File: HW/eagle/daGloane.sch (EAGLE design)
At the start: 110 parts, among them IC1 MCP1252-33X50, U1 STM32F10XTXU6, X2 SPARKFUN-CONNECTORS_USB-MICROB

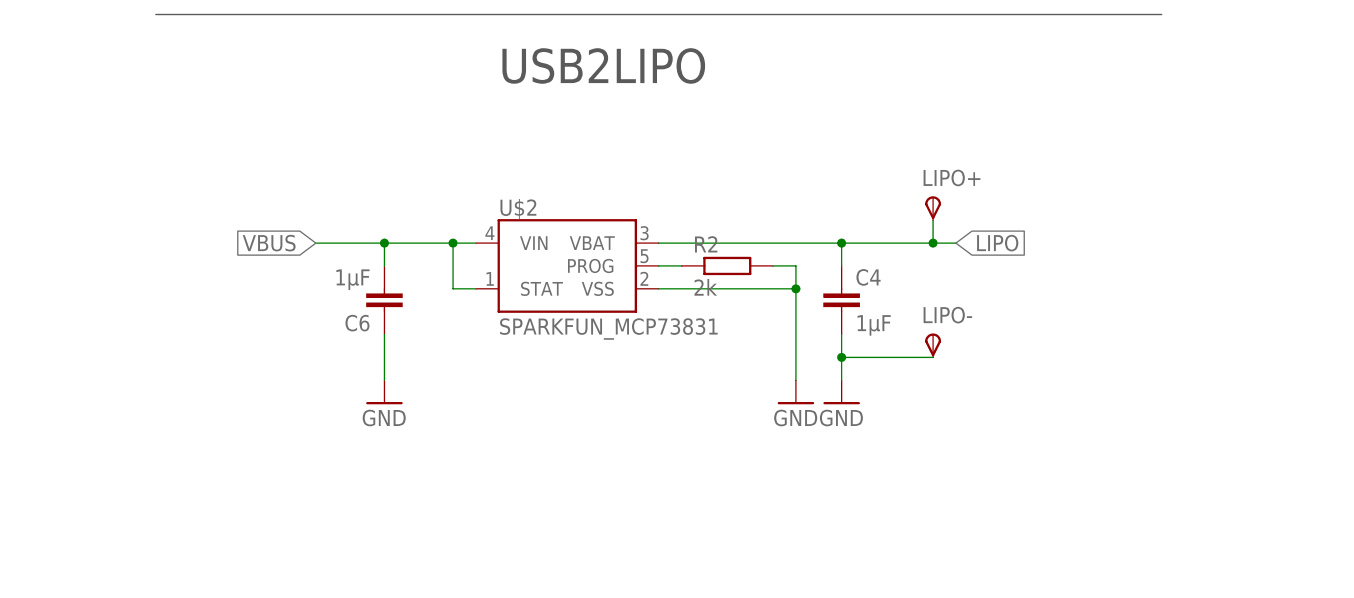
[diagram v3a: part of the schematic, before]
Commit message: led added to LiPo charge IC
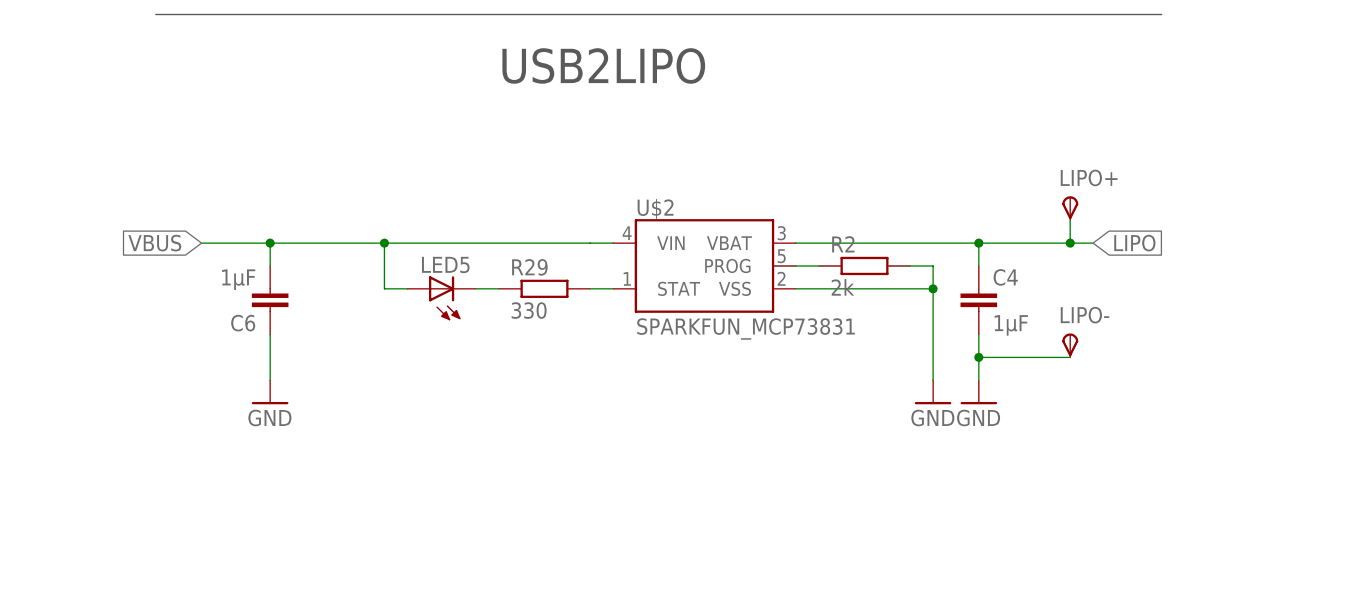
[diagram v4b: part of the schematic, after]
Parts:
- added LED5: (no value), led:LEDCHIPLED_0805
- added R29: 330, rcl:R-EU_R0603
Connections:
- new net N$43: R29.2, U$2.STAT
- new net N$44: LED5.C, R29.1
- net VBUS: now also LED5.A; no longer U$2.STAT
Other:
- moved on the sheet: C4, C6, LIPO+, LIPO-, R2, U$2
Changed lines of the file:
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@@
 <part name="R28" library="rcl" deviceset="R-EU_" device="R0603" value="10k"/>
 <part name="D5" library="diode" deviceset="MBR0520LT" device=""/>
+<part name="LED5" library="led" deviceset="LED" device="CHIPLED_0805"/>
+<part name="R29" library="rcl" deviceset="R-EU_" device="R0603" value="330"/>
 </parts>
 <sheets>
@@
 <instance part="LED1" gate="G$1" x="149.86" y="-355.6" rot="R270"/>
 <instance part="LED2" gate="G$1" x="149.86" y="-365.76" rot="R270"/>
-<instance part="U$2" gate="G$1" x="68.58" y="-167.64"/>
-<instance part="C6" gate="G$1" x="48.26" y="-172.72" rot="R180"/>
-<instance part="GND28" gate="1" x="48.26" y="-182.88"/>
-<instance part="GND29" gate="1" x="93.98" y="-182.88"/>
-<instance part="C4" gate="G$1" x="99.06" y="-170.18"/>
-<instance part="GND30" gate="1" x="99.06" y="-182.88"/>
-<instance part="LIPO+" gate="G$1" x="109.22" y="-160.02"/>
-<instance part="LIPO-" gate="G$1" x="109.22" y="-175.26"/>
-<instance part="R2" gate="G$1" x="86.36" y="-167.64"/>
+<instance part="U$2" gate="G$1" x="83.82" y="-167.64"/>
+<instance part="C6" gate="G$1" x="35.56" y="-172.72" rot="R180"/>
+<instance part="GND28" gate="1" x="35.56" y="-182.88"/>
+<instance part="GND29" gate="1" x="109.22" y="-182.88"/>
+<instance part="C4" gate="G$1" x="114.3" y="-170.18"/>
+<instance part="GND30" gate="1" x="114.3" y="-182.88"/>
+<instance part="LIPO+" gate="G$1" x="124.46" y="-160.02"/>
+<instance part="LIPO-" gate="G$1" x="124.46" y="-175.26"/>
+<instance part="R2" gate="G$1" x="101.6" y="-167.64"/>
 <instance part="IC1" gate="G$1" x="218.44" y="-78.74"/>
 <instance part="C13" gate="G$1" x="243.84" y="-81.28"/>
@@
 <instance part="R28" gate="G$1" x="462.28" y="-340.36"/>
 <instance part="D5" gate="G$1" x="472.44" y="-317.5" rot="R90"/>
+<instance part="LED5" gate="G$1" x="53.34" y="-170.18" rot="R90"/>
+<instance part="R29" gate="G$1" x="66.04" y="-170.18"/>
 </instances>
 <busses>
@@
 <pinref part="C6" gate="G$1" pin="1"/>
 <pinref part="GND28" gate="1" pin="GND"/>
-<wire x1="48.26" y1="-180.34" x2="48.26" y2="-175.26" width="0.1524" layer="91"/>
+<wire x1="35.56" y1="-180.34" x2="35.56" y2="-175.26" width="0.1524" layer="91"/>
 </segment>
 <segment>
-<wire x1="93.98" y1="-167.64" x2="93.98" y2="-170.18" width="0.1524" layer="91"/>
+<wire x1="109.22" y1="-167.64" x2="109.22" y2="-170.18" width="0.1524" layer="91"/>
 <pinref part="U$2" gate="G$1" pin="VSS"/>
-<wire x1="78.74" y1="-170.18" x2="93.98" y2="-170.18" width="0.1524" layer="91"/>
-<wire x1="93.98" y1="-170.18" x2="93.98" y2="-180.34" width="0.1524" layer="91"/>
-<junction x="93.98" y="-170.18"/>
+<wire x1="93.98" y1="-170.18" x2="109.22" y2="-170.18" width="0.1524" layer="91"/>
+<wire x1="109.22" y1="-170.18" x2="109.22" y2="-180.34" width="0.1524" layer="91"/>
+<junction x="109.22" y="-170.18"/>
 <pinref part="GND29" gate="1" pin="GND"/>
 <pinref part="R2" gate="G$1" pin="2"/>
-<wire x1="91.44" y1="-167.64" x2="93.98" y2="-167.64" width="0.1524" layer="91"/>
+<wire x1="106.68" y1="-167.64" x2="109.22" y2="-167.64" width="0.1524" layer="91"/>
 </segment>
 <segment>
 <pinref part="GND30" gate="1" pin="GND"/>
 <pinref part="C4" gate="G$1" pin="2"/>
-<wire x1="99.06" y1="-180.34" x2="99.06" y2="-177.8" width="0.1524" layer="91"/>
+<wire x1="114.3" y1="-180.34" x2="114.3" y2="-177.8" width="0.1524" layer="91"/>
 <pinref part="LIPO-" gate="G$1" pin="PP"/>
-<wire x1="99.06" y1="-177.8" x2="99.06" y2="-175.26" width="0.1524" layer="91"/>
-<wire x1="109.22" y1="-177.8" x2="99.06" y2="-177.8" width="0.1524" layer="91"/>
-<junction x="99.06" y="-177.8"/>
+<wire x1="114.3" y1="-177.8" x2="114.3" y2="-175.26" width="0.1524" layer="91"/>
+<wire x1="124.46" y1="-177.8" x2="114.3" y2="-177.8" width="0.1524" layer="91"/>
+<junction x="114.3" y="-177.8"/>
 </segment>
 <segment>
@@
 <segment>
 <pinref part="C4" gate="G$1" pin="1"/>
-<wire x1="99.06" y1="-167.64" x2="99.06" y2="-165.1" width="0.1524" layer="91"/>
+<wire x1="114.3" y1="-167.64" x2="114.3" y2="-165.1" width="0.1524" layer="91"/>
 <pinref part="U$2" gate="G$1" pin="VBAT"/>
-<wire x1="99.06" y1="-165.1" x2="78.74" y2="-165.1" width="0.1524" layer="91"/>
-<wire x1="99.06" y1="-165.1" x2="109.22" y2="-165.1" width="0.1524" layer="91"/>
-<junction x="99.06" y="-165.1"/>
-<label x="111.76" y="-165.1" size="1.778" layer="95" xref="yes"/>
+<wire x1="114.3" y1="-165.1" x2="93.98" y2="-165.1" width="0.1524" layer="91"/>
+<wire x1="114.3" y1="-165.1" x2="124.46" y2="-165.1" width="0.1524" layer="91"/>
+<junction x="114.3" y="-165.1"/>
+<label x="127" y="-165.1" size="1.778" layer="95" xref="yes"/>
 <pinref part="LIPO+" gate="G$1" pin="PP"/>
-<wire x1="109.22" y1="-165.1" x2="111.76" y2="-165.1" width="0.1524" layer="91"/>
-<wire x1="109.22" y1="-162.56" x2="109.22" y2="-165.1" width="0.1524" layer="91"/>
-<junction x="109.22" y="-165.1"/>
+<wire x1="124.46" y1="-165.1" x2="127" y2="-165.1" width="0.1524" layer="91"/>
+<wire x1="124.46" y1="-162.56" x2="124.46" y2="-165.1" width="0.1524" layer="91"/>
+<junction x="124.46" y="-165.1"/>
 </segment>
 <segment>
@@
 </segment>
 <segment>
-<pinref part="U$2" gate="G$1" pin="STAT"/>
-<wire x1="58.42" y1="-170.18" x2="55.88" y2="-170.18" width="0.1524" layer="91"/>
-<wire x1="55.88" y1="-170.18" x2="55.88" y2="-165.1" width="0.1524" layer="91"/>
 <pinref part="U$2" gate="G$1" pin="VIN"/>
-<wire x1="55.88" y1="-165.1" x2="58.42" y2="-165.1" width="0.1524" layer="91"/>
-<wire x1="55.88" y1="-165.1" x2="48.26" y2="-165.1" width="0.1524" layer="91"/>
-<junction x="55.88" y="-165.1"/>
+<wire x1="71.12" y1="-165.1" x2="73.66" y2="-165.1" width="0.1524" layer="91"/>
+<wire x1="71.12" y1="-165.1" x2="48.26" y2="-165.1" width="0.1524" layer="91"/>
 <pinref part="C6" gate="G$1" pin="2"/>
-<wire x1="48.26" y1="-165.1" x2="48.26" y2="-167.64" width="0.1524" layer="91"/>
-<wire x1="48.26" y1="-165.1" x2="40.64" y2="-165.1" width="0.1524" layer="91"/>
+<wire x1="48.26" y1="-165.1" x2="35.56" y2="-165.1" width="0.1524" layer="91"/>
+<wire x1="35.56" y1="-165.1" x2="35.56" y2="-167.64" width="0.1524" layer="91"/>
+<wire x1="35.56" y1="-165.1" x2="27.94" y2="-165.1" width="0.1524" layer="91"/>
+<junction x="35.56" y="-165.1"/>
+<label x="27.94" y="-165.1" size="1.778" layer="95" rot="R180" xref="yes"/>
+<pinref part="LED5" gate="G$1" pin="A"/>
+<wire x1="50.8" y1="-170.18" x2="48.26" y2="-170.18" width="0.1524" layer="91"/>
+<wire x1="48.26" y1="-170.18" x2="48.26" y2="-165.1" width="0.1524" layer="91"/>
 <junction x="48.26" y="-165.1"/>
-<label x="40.64" y="-165.1" size="1.778" layer="95" rot="R180" xref="yes"/>
 </segment>
 </net>
@@
 <pinref part="U$2" gate="G$1" pin="PROG"/>
 <pinref part="R2" gate="G$1" pin="1"/>
-<wire x1="81.28" y1="-167.64" x2="78.74" y2="-167.64" width="0.1524" layer="91"/>
+<wire x1="96.52" y1="-167.64" x2="93.98" y2="-167.64" width="0.1524" layer="91"/>
 </segment>
 </net>
@@
 </segment>
 </net>
+<net name="N$43" class="0">
+<segment>
+<pinref part="U$2" gate="G$1" pin="STAT"/>
+<pinref part="R29" gate="G$1" pin="2"/>
+<wire x1="71.12" y1="-170.18" x2="73.66" y2="-170.18" width="0.1524" layer="91"/>
+</segment>
+</net>
+<net name="N$44" class="0">
+<segment>
+<pinref part="R29" gate="G$1" pin="1"/>
+<pinref part="LED5" gate="G$1" pin="C"/>
+<wire x1="58.42" y1="-170.18" x2="60.96" y2="-170.18" width="0.1524" layer="91"/>
+</segment>
+</net>

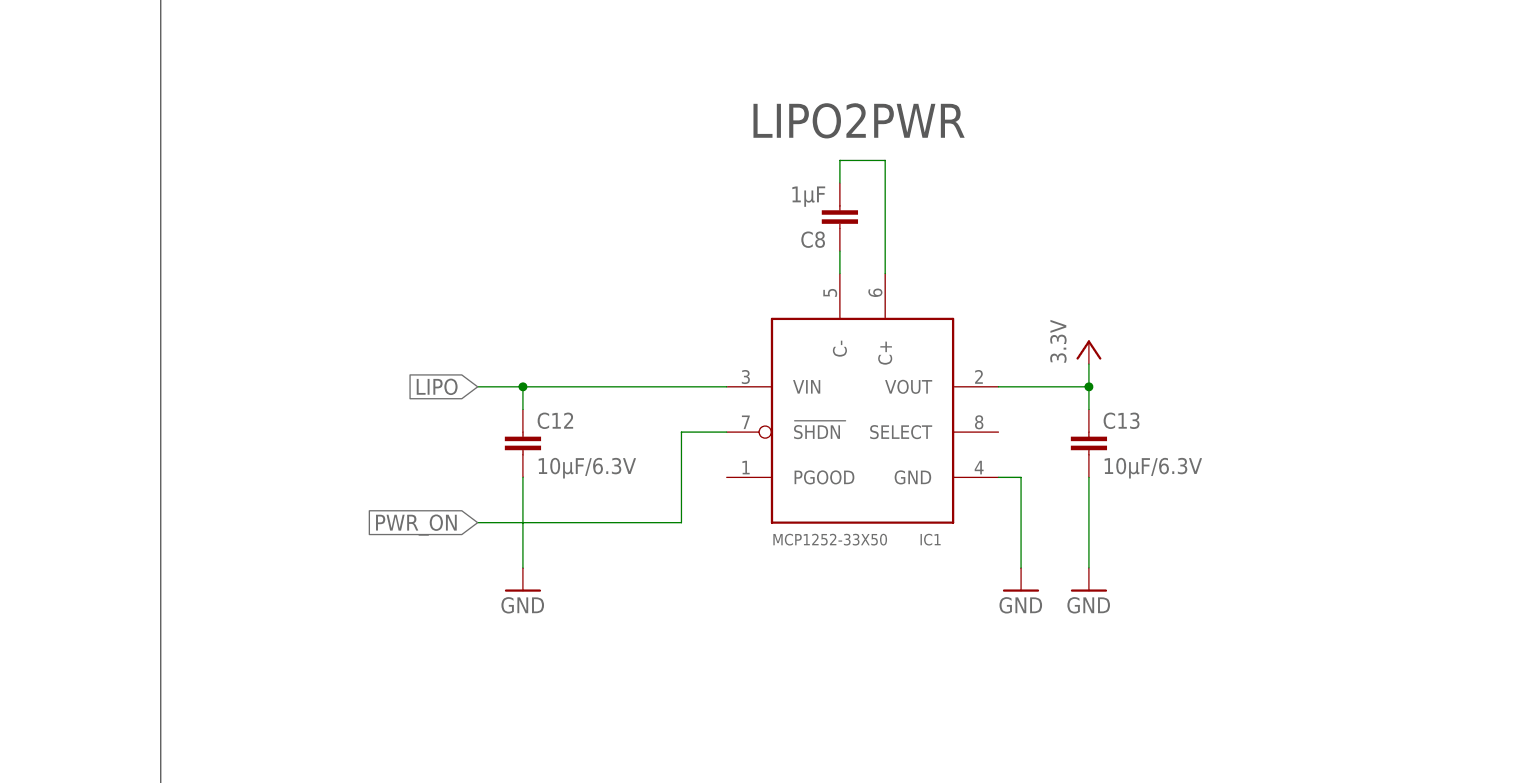
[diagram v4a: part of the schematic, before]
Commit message: - PI filter added to charge pump DC/DC - trough hole pads for BLDC motors replaced with SMT type pads
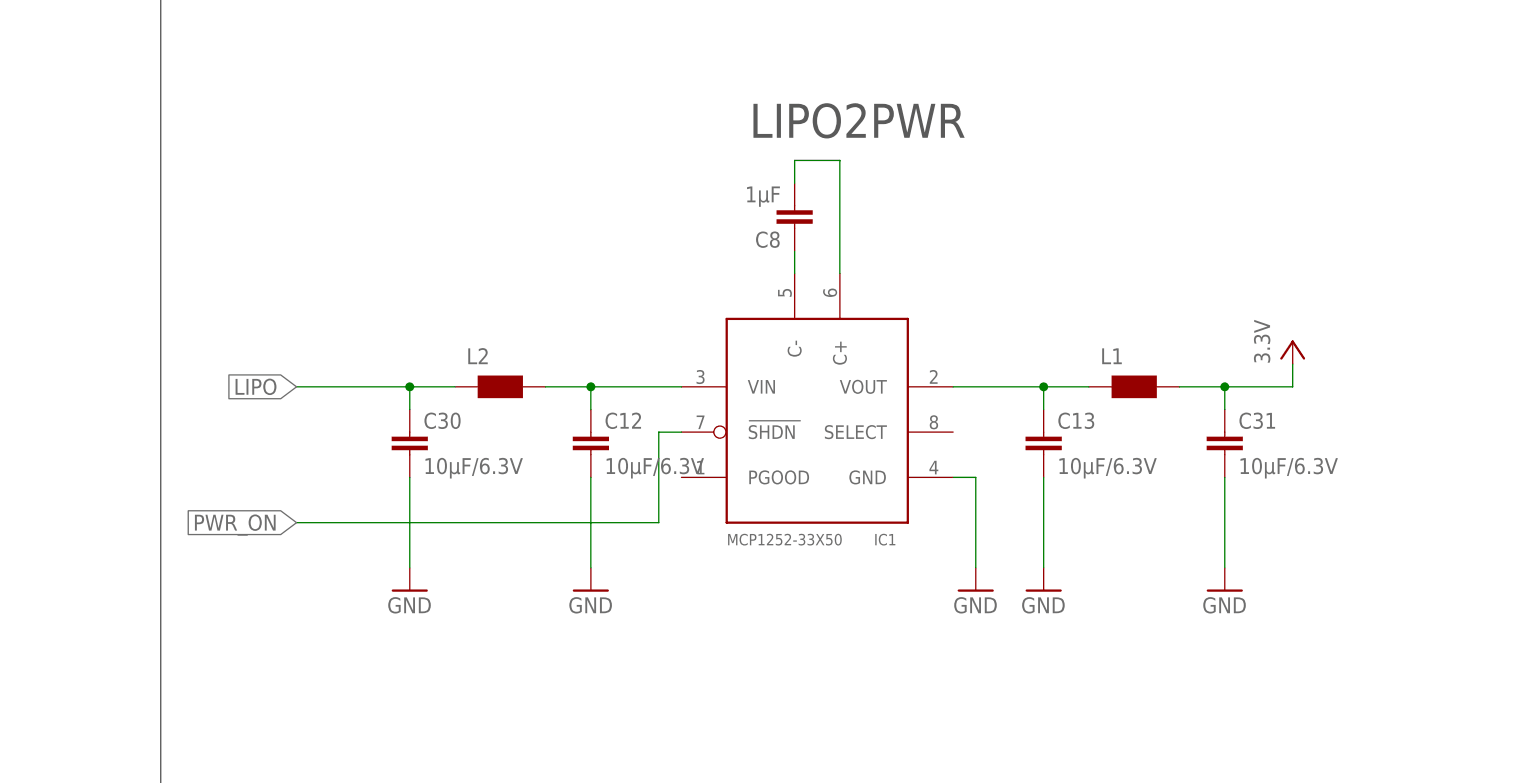
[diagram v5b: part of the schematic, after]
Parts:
- added C30, C31: 10µF/6.3V, rcl:C-EUC0805
- added L1, L2: (no value), daGloane:WUERTH-ELEKTRONIK_WE-KI_0805_B
- MOT1_A, MOT1_B, MOT1_C, MOT2_A, MOT2_B, MOT2_C, MOT3_A, MOT3_B, MOT3_C, MOT4_A, MOT4_B, MOT4_C: value WIREPAD1,6/0,8 -> WIREPADSMD1,27-254; device wirepad:WIREPAD1,6/0,8 -> wirepad:WIREPADSMD1,27-254
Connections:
- new net N$45: C12.1, IC1.VIN, L2.2
- new net N$46: C13.1, IC1.VOUT, L1.1
- net GND: now also C30.2, C31.2
- net LIPO: now also C30.1, L2.1; no longer C12.1, IC1.VIN
- net VCC: now also C31.1, L1.2; no longer C13.1, IC1.VOUT
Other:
- moved on the sheet: C12, C13, C8, IC1

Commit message: 100nF capacitor added to PI filters of charge pump dc/dc series resistors of spi resized to 150R
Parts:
- removed R18: 3k3, rcl:R-EU_R0603
- added C32, C33: 100nF, rcl:C-EUC0603
- LED1, LED2, LED3, LED4, LED5: device led:LEDCHIPLED_0805 -> led:LEDCHIPLED_0603
- R1, R3, R4, R5: value 1k -> 150R
- R17: value 3k3 -> 10k
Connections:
- removed net N$22: C20.1, R12.1, R18.2, R21.2
- net GND: now also C32.1, C33.1
- net LIPO: now also C32.2
- net VCC: now also C33.2
- net VOLTAGE: now also C20.1, R12.1, R21.2; no longer R18.1
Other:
- note removed: "Filter hinter charge pump?"
- moved on the sheet: C13, C30, C31, L1

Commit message: bootmode jumper replaced with 50mil pitch type
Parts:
- BOOTMD: device SparkFun:JUMPER-2PTH -> daGloane:JUMPER-2
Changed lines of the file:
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@@
 <?xml version="1.0" encoding="utf-8"?>
 <!DOCTYPE eagle SYSTEM "eagle.dtd">
-<eagle version="6.1">
+<eagle version="6.2">
 <drawing>
 <settings>
@@
 <part name="C20" library="rcl" deviceset="C-EU" device="C0603" value="100nF"/>
 <part name="R15" library="rcl" deviceset="R-EU_" device="R0603" value="150R"/>
-<part name="BOOTMD" library="SparkFun" deviceset="JUMPER-2" device="PTH"/>
+<part name="BOOTMD" library="daGloane" deviceset="JUMPER-2" device=""/>
 <part name="GND41" library="supply1" deviceset="GND" device=""/>
 <part name="GND43" library="supply1" deviceset="GND" device=""/>

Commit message: cosmetic changes
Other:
- note added: "Micro-USB-B"
- note removed: "Mini-USB-B"
- note removed: "MotorTreiber: MTD6505?"
- moved on the sheet: BOOTMD, C12, C13, C16, C17, C18, C19, C21, C22, C23, C24, C25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
